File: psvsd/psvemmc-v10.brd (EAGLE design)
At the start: 41 x 22.5 mm, 40 parts, among them U1 USB2244QFN, U2 LP3996_DSC_10, U3 LSF0204RUTR, U4 LSF0204RUTR, U5 LSF0204RUTR, X1 ZX62D-B-5PA8, Y1 XRCGB

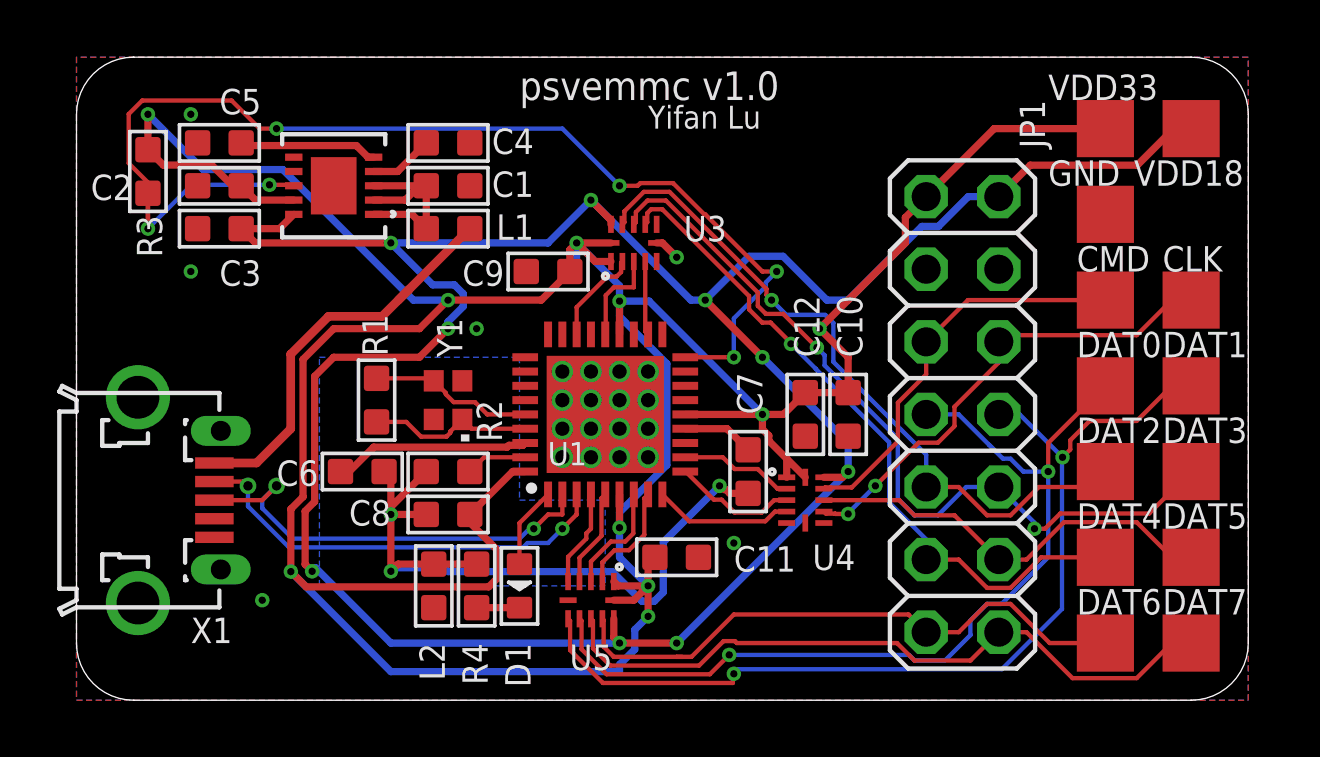
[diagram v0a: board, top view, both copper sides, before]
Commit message: psvemmc v1.1: fixed missing caps for crystal and fixed direction of translator
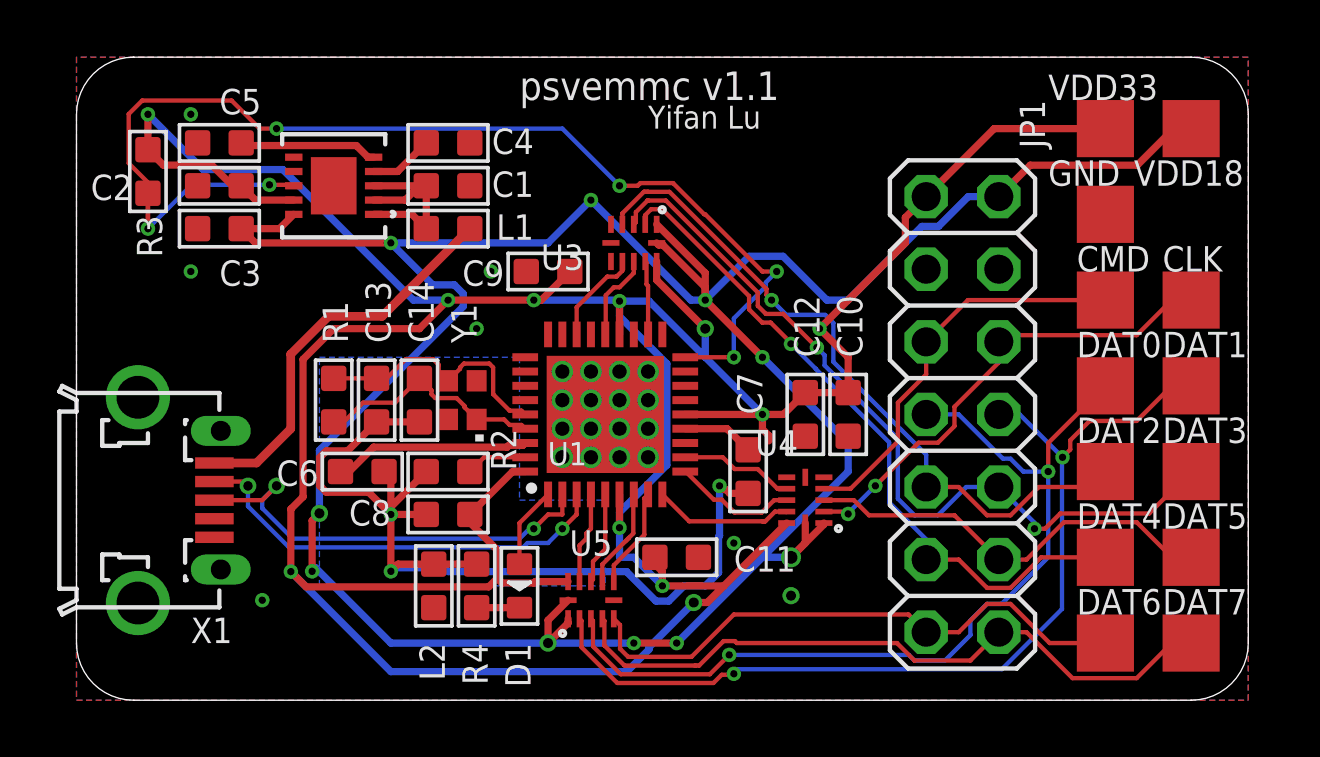
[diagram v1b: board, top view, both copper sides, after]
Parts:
- added C13, C14: 10pf, Seeed-Capacitor:C0603
- moved R1 1.50 mm to (9.00, 10.5)
- moved Y1 0.50 mm to (13.5, 10.5)
- turned U3 to 180 degrees
- turned U4 to 90 degrees
- turned U5 to 0 degrees
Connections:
- net GNDA: now also C13.1, C14.2
- net MMC_CLK: now also U4.2; no longer U4.8
- net MMC_CMD: now also U4.4; no longer U4.10
- net MMC_D0: now also U5.3; no longer U5.8
- net MMC_D1: now also U5.2; no longer U5.7
- net MMC_D2: now also U3.4; no longer U3.10
- net MMC_D3: now also U3.3; no longer U3.9
- net MMC_D4: now also U3.2; no longer U3.8
- net MMC_D5: now also U4.3; no longer U4.9
- net MMC_D6: now also U5.5; no longer U5.10
- net MMC_D7: now also U5.4; no longer U5.9
- net SD_CLK: now also U4.10; no longer U4.4
- net SD_CMD: now also U4.8; no longer U4.2
- net SD_D0: now also U5.9; no longer U5.4
- net SD_D1: now also U5.10; no longer U5.5
- net SD_D2: now also U3.8; no longer U3.2
- net SD_D3: now also U3.9; no longer U3.3
- net SD_D4: now also U3.10; no longer U3.4
- net SD_D5: now also U4.9; no longer U4.3
- net SD_D6: now also U5.7; no longer U5.2
- net SD_D7: now also U5.8; no longer U5.3
- net VDD18: now also U3.1, U3.12, U4.1, U4.12, U5.1, U5.12; no longer U3.11, U4.11, U5.11
- net VDD33: now also U3.11, U4.11, U5.11; no longer U3.1, U3.12, U4.1, U4.12, U5.1, U5.12
- net XTAL1: now also C14.1
- net XTAL2: now also C13.2
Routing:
- net GNDA: track 26.2 -> 34.9 mm
- net VDD18: track 91.9 -> 100.1 mm, vias 9 -> 10
- net VDD33: track 125.1 -> 129.7 mm, vias 10 -> 11
- net XTAL2: track 5.75 -> 8.99 mm
- net XTAL1: track 5.83 -> 8.17 mm
- net GND: track 1.61 -> 0.71 mm, vias 22 -> 23
- net MMC_D0: track 32.2 -> 31.4 mm
- net MMC_D6: track 20.7 -> 20.1 mm
- net MMC_D1: track 33.9 -> 33.3 mm
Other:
- board text added: "psvemmc v1.1"
- board text removed: "psvemmc v1.0"
